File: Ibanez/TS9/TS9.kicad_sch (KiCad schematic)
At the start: 33 parts, among them Q1 2N3904, Q2 2N3904, U1 NJM4558

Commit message: feat: フットプリントを紐づけ
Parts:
- added C10, C11: 100u, Capacitor_THT:CP_Radial_D8.0mm_P3.50mm, symbol Device:C_Polarized
- added D3: 1N4001, Diode_THT:D_DO-41_SOD81_P7.62mm_Horizontal, symbol Diode:1N4001
- added D4: LED, LED_THT:LED_D5.0mm, symbol Device:LED
- added J1: I/O, Connector_PinHeader_2.54mm:PinHeader_1x03_P2.54mm_Vertical, symbol Connector:Conn_01x03_Pin
- added J2, J3: Power, Connector_PinHeader_2.54mm:PinHeader_1x02_P2.54mm_Vertical, symbol Connector:Conn_01x02_Pin
- added R17: 100R, Resistor_THT:R_Axial_DIN0207_L6.3mm_D2.5mm_P7.62mm_Horizontal, symbol Device:R
- added R18, R19, R20: 10k, Resistor_THT:R_Axial_DIN0207_L6.3mm_D2.5mm_P7.62mm_Horizontal, symbol Device:R
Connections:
- net GND: now also U1.4 (V-), C10.2, C11.2, D3.2 (A), J1.3 (Pin_3), J2.2 (Pin_2), J3.2 (Pin_2), R20.1
- net INPUT: now also J1.1 (Pin_1)
- net NEUT: now also C11.1, R19.2, R20.2
- net OUTPUT: now also J1.2 (Pin_2)
- net at U1.8 (V+): now also C10.1, R17.2, R19.1
- new net: D4.2 (A), R18.2
- new net +9V: D3.1 (K), J2.1 (Pin_1), R17.1, R18.1
- new net LED: D4.1 (K), J3.1 (Pin_1)
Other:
- title: (none) -> Ibanez - TS9
- moved on the sheet: C1, C2, C3, C4, C5, C6, C7, C8, C9, Q1, Q2, R1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

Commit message: feat: フットプリントを紐づけ
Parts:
- removed C2, C7: 1u, symbol Device:C
- added C12: 1u, Capacitor_THT:CP_Radial_D5.0mm_P2.00mm, symbol Device:C_Polarized
- added C13: 10u, Capacitor_THT:CP_Radial_D5.0mm_P2.00mm, symbol Device:C_Polarized
- C1: footprint (none) -> Capacitor_THT:C_Rect_L7.2mm_W3.0mm_P5.00mm_FKS2_FKP2_MKS2_MKP2
- C10: renamed from C8; footprint (none) -> Capacitor_THT:C_Rect_L10.3mm_W5.7mm_P7.50mm_MKS4
- C11: renamed from C9; value C_Polarized -> 10u; footprint (none) -> Capacitor_THT:CP_Radial_D5.0mm_P2.00mm
- C5: renamed from C4; footprint (none) -> Capacitor_THT:C_Rect_L7.2mm_W3.0mm_P5.00mm_FKS2_FKP2_MKS2_MKP2
- C6: renamed from C3; footprint (none) -> Capacitor_THT:C_Disc_D3.8mm_W2.6mm_P2.50mm
- C7: renamed from C5; footprint (none) -> Capacitor_THT:C_Rect_L10.3mm_W5.7mm_P7.50mm_MKS4
- C8: renamed from C6; footprint (none) -> Capacitor_THT:C_Rect_L10.3mm_W5.7mm_P7.50mm_MKS4
- R1: renamed from R8; footprint (none) -> Resistor_THT:R_Axial_DIN0207_L6.3mm_D2.5mm_P7.62mm_Horizontal
- R10: renamed from R4; footprint (none) -> Resistor_THT:R_Axial_DIN0207_L6.3mm_D2.5mm_P7.62mm_Horizontal
- R11: renamed from R5; footprint (none) -> Resistor_THT:R_Axial_DIN0207_L6.3mm_D2.5mm_P7.62mm_Horizontal
- R12: renamed from R7; footprint (none) -> Resistor_THT:R_Axial_DIN0207_L6.3mm_D2.5mm_P7.62mm_Horizontal
- R13: renamed from R10; footprint (none) -> Resistor_THT:R_Axial_DIN0207_L6.3mm_D2.5mm_P7.62mm_Horizontal
- R14: renamed from R9; footprint (none) -> Resistor_THT:R_Axial_DIN0207_L6.3mm_D2.5mm_P7.62mm_Horizontal
- R15: renamed from R11; footprint (none) -> Resistor_THT:R_Axial_DIN0207_L6.3mm_D2.5mm_P7.62mm_Horizontal
- R16: renamed from R12; footprint (none) -> Resistor_THT:R_Axial_DIN0207_L6.3mm_D2.5mm_P7.62mm_Horizontal
- R17: renamed from R13; footprint (none) -> Resistor_THT:R_Axial_DIN0207_L6.3mm_D2.5mm_P7.62mm_Horizontal
- R18: renamed from R14; footprint (none) -> Resistor_THT:R_Axial_DIN0207_L6.3mm_D2.5mm_P7.62mm_Horizontal
- R19: renamed from R15; footprint (none) -> Resistor_THT:R_Axial_DIN0207_L6.3mm_D2.5mm_P7.62mm_Horizontal
- R20: renamed from R16; footprint (none) -> Resistor_THT:R_Axial_DIN0207_L6.3mm_D2.5mm_P7.62mm_Horizontal
- R3: renamed from R1; footprint (none) -> Resistor_THT:R_Axial_DIN0207_L6.3mm_D2.5mm_P7.62mm_Horizontal
- R5: renamed from R2; footprint (none) -> Resistor_THT:R_Axial_DIN0207_L6.3mm_D2.5mm_P7.62mm_Horizontal
- R8: renamed from R3; footprint (none) -> Resistor_THT:R_Axial_DIN0207_L6.3mm_D2.5mm_P7.62mm_Horizontal
- R9: renamed from R6; footprint (none) -> Resistor_THT:R_Axial_DIN0207_L6.3mm_D2.5mm_P7.62mm_Horizontal
- RV1: renamed from RV3; footprint (none) -> Potentiometer_THT:Potentiometer_Omeg_PC16BU_Vertical
- RV2: footprint (none) -> Potentiometer_THT:Potentiometer_Omeg_PC16BU_Vertical
- RV3: renamed from RV1; footprint (none) -> Potentiometer_THT:Potentiometer_Omeg_PC16BU_Vertical
- U1: footprint (none) -> Package_DIP:DIP-8_W10.16mm
- renumbered C10 to C2, C11 to C3, D3 to D1, D4 to D2, D2 to D3, D1 to D4, R17 to R2, R18 to R4, R19 to R6, R20 to R7
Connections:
- net at R10.2, U1.3 (+): now also C12.2
- net at Q1.1 (E), R8.2: now also C12.1
- net at R15.2, U1.7: now also C13.1
- net at R16.1: now also C13.2

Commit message: refactor: 見直しに伴う形式的な更新
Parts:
- renumbered C12 to C4, C13 to C9
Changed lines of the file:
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@@
 		(dnp no)
 		(fields_autoplaced yes)
-		(property "Reference" "C12"
+		(property "Reference" "C4"
 			(at 88.011 81.28 90)
 			(show_name no)
@@
 			(project "TS9"
 				(path "/7a474f6e-d8dd-42e4-9321-d1e94f717f3f"
-					(reference "C12")
+					(reference "C4")
 					(unit 1)
 				)
@@
 		(dnp no)
 		(fields_autoplaced yes)
-		(property "Reference" "C13"
+		(property "Reference" "C9"
 			(at 176.911 68.58 90)
 			(show_name no)
@@
 			(project "TS9"
 				(path "/7a474f6e-d8dd-42e4-9321-d1e94f717f3f"
-					(reference "C13")
-					(unit 1)
-				)
+					(reference "C9")
+					(unit 1)
+				)

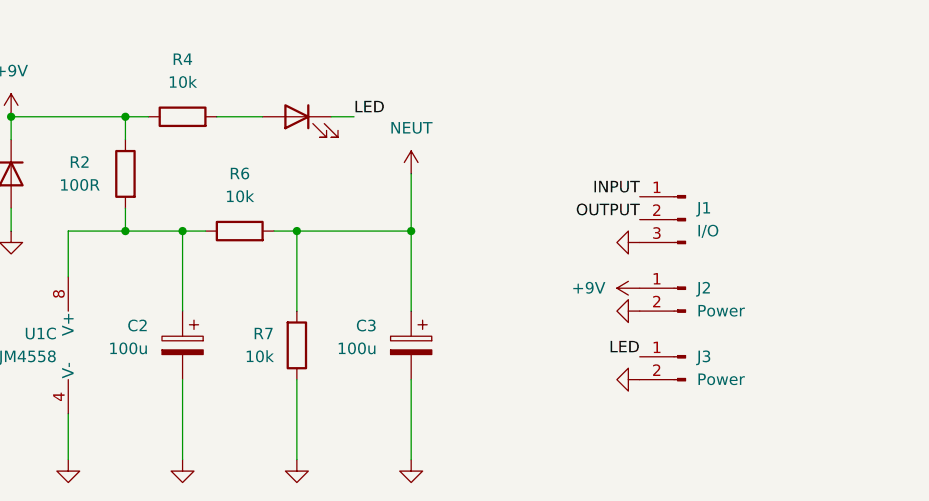
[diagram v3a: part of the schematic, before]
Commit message: feat: ReLayout Ibanez/TS9
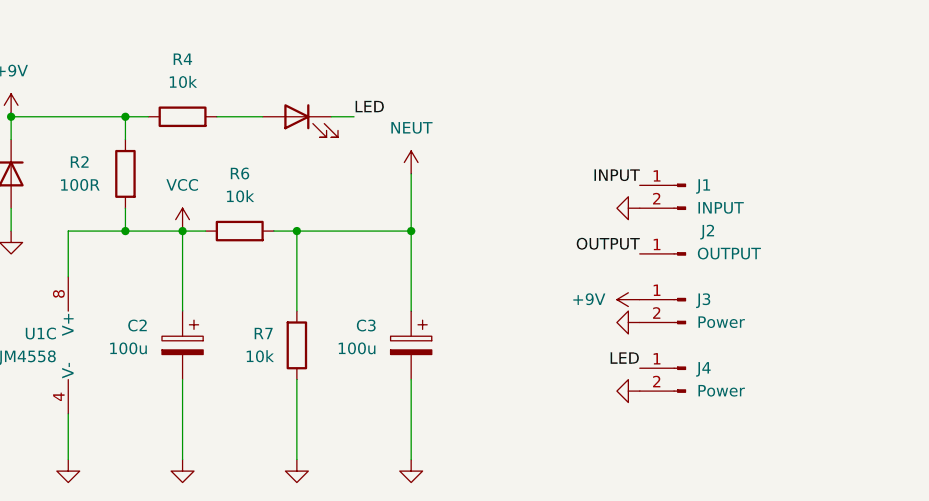
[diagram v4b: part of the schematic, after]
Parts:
- removed J1: I/O, Connector_PinHeader_2.54mm:PinHeader_1x03_P2.54mm_Vertical, symbol Connector:Conn_01x03_Pin
- added J1: INPUT, Connector_PinHeader_2.54mm:PinHeader_1x02_P2.54mm_Vertical, symbol Connector:Conn_01x02_Pin
- added J2: OUTPUT, Connector_PinHeader_2.54mm:PinHeader_1x01_P2.54mm_Vertical, symbol Connector:Conn_01x01_Pin
- D3, D4: footprint Diode_THT:D_DO-35_SOD27_P7.62mm_Horizontal -> Diode_THT:D_DO-35_SOD27_P5.08mm_Vertical_AnodeUp
- Q1, Q2: footprint Package_TO_SOT_THT:TO-92_Inline -> Package_TO_SOT_THT:TO-92_Inline_Wide
- U1: footprint Package_DIP:DIP-8_W10.16mm -> Package_DIP:DIP-8_W7.62mm
- renumbered J2 to J3, J3 to J4
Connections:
- net GND: now also J1.2 (Pin_2)
- net INPUT: now also J1.1 (Pin_1)
- net OUTPUT: now also J2.1 (Pin_1)
- net VCC: now also C2.1, R2.2, R6.1, U1.8 (V+)
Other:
- moved on the sheet: J3, J4
